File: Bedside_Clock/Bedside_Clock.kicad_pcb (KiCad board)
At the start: 4 copper layers, 177.8 x 68.6 mm, 213 parts, among them J1 USBC_USB2.0, SW1 COLOR, SW2 MODE, SW3 BOOT, SW4 RESET, U1 ESP32-C3-MINI-1, U2 USBLC6-2SC6, U3 VCNL4040M3OE, U4 SN74LVC2T45DCTR, U5 MCP1825S

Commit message: [Docs] Add Schematics and Renders Add Diodes, Switches, and Conns to BOM Need Resistors and Capacitors now
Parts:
- R5: value 1k3 -> 1k43
- moved R10 0.25 mm to (120.6, 71.4)
- moved R11 0.25 mm to (123.6, 71.4)
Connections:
- net Net-(J1-CC2) renamed /CC2
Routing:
- net +3V3: track 83.4 -> 84.2 mm
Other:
- board text added: "3V3"
- board text added: "5V"
- board text added: "GND"
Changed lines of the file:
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@@
 	(net 186 "Net-(D87-Pad2)")
 	(net 187 "/CC1")
-	(net 188 "Net-(J1-CC2)")
+	(net 188 "/CC2")
 	(net 189 "Net-(U1-GPIO8)")
 	(net 190 "/LED_BUILTIN")
@@
 			(size 0.3 1.1)
 			(layers "F.Cu" "F.Mask" "F.Paste")
-			(net 188 "Net-(J1-CC2)")
+			(net 188 "/CC2")
 			(pinfunction "CC2")
 			(pintype "bidirectional")
@@
 			(layers "F.Cu" "F.Mask" "F.Paste")
 			(roundrect_rratio 0.25)
-			(net 188 "Net-(J1-CC2)")
+			(net 188 "/CC2")
 			(pintype "passive")
 		)
@@
 			)
 		)
-		(property "Value" "1k3"
+		(property "Value" "1k43"
 			(at 0 -1.43 90)
 			(layer "B.Fab")
@@
 	(footprint "Resistor_SMD:R_0603_1608Metric"
 		(layer "B.Cu")
-		(at 120.587 71.628 180)
+		(at 120.587 71.374 180)
 		(descr "Resistor SMD 0603 (1608 Metric), square (rectangular) end terminal, IPC-7351 nominal, (Body size source: IPC-SM-782 page 72, https://www.pcb-3d.com/wordpress/wp-content/uploads/ipc-sm-782a_amendment_1_and_2.pdf), generated with kicad-footprint-generator")
 		(tags "resistor")
@@
 	(footprint "Resistor_SMD:R_0603_1608Metric"
 		(layer "B.Cu")
-		(at 123.634 71.628)
+		(at 123.634 71.374)
 		(descr "Resistor SMD 0603 (1608 Metric), square (rectangular) end terminal, IPC-7351 nominal, (Body size source: IPC-SM-782 page 72, https://www.pcb-3d.com/wordpress/wp-content/uploads/ipc-sm-782a_amendment_1_and_2.pdf), generated with kicad-footprint-generator")
 		(tags "resistor")
@@
 		(layer "User.2")
 	)
+	(gr_text "GND"
+		(at 116.0272 70.231 0)
+		(layer "B.SilkS")
+		(effects
+			(font
+				(size 1 1)
+				(thickness 0.15)
+			)
+			(justify right mirror)
+		)
+	)
+	(gr_text "3V3"
+		(at 116.0272 72.531 0)
+		(layer "B.SilkS")
+		(effects
+			(font
+				(size 1 1)
+				(thickness 0.15)
+			)
+			(justify right mirror)
+		)
+	)
+	(gr_text "5V"
+		(at 116.0272 67.931 0)
+		(layer "B.SilkS")
+		(effects
+			(font
+				(size 1 1)
+				(thickness 0.15)
+			)
+			(justify right mirror)
+		)
+	)
 	(segment
 		(start 133.78 50.66)
@@
 	)
 	(via
-		(at 125.349 71.628)
+		(at 125.222 71.374)
 		(size 0.6)
 		(drill 0.3)
@@
 	)
 	(via
-		(at 118.872 71.628)
+		(at 118.999 71.374)
 		(size 0.6)
 		(drill 0.3)
@@
 	)
 	(segment
-		(start 118.872 71.628)
-		(end 119.762 71.628)
+		(start 117.348 69.469)
+		(end 117.348 58.293)
+		(width 0.4)
+		(layer "B.Cu")
+		(net 181)
+	)
+	(segment
+		(start 124.459 71.374)
+		(end 125.222 71.374)
+		(width 0.4)
+		(layer "B.Cu")
+		(net 181)
+	)
+	(segment
+		(start 117.348 70.118)
+		(end 117.348 69.469)
+		(width 0.4)
+		(layer "B.Cu")
+		(net 181)
+	)
+	(segment
+		(start 114.935 72.531)
+		(end 117.842 72.531)
 		(width 0.4)
 		(layer "B.Cu")
@@
 	)
 	(segment
-		(start 119.448 54.356)
-		(end 117.869 54.356)
+		(start 117.348 69.977)
+		(end 117.348 69.723)
 		(width 0.4)
 		(layer "B.Cu")
@@
 	)
 	(segment
-		(start 117.969 72.531)
-		(end 114.935 72.531)
+		(start 117.348 69.723)
+		(end 117.348 69.469)
 		(width 0.4)
 		(layer "B.Cu")
@@
 	)
 	(segment
-		(start 87.995 85.699)
-		(end 87.995 84.104)
+		(start 119.448 54.356)
+		(end 117.869 54.356)
 		(width 0.4)
 		(layer "B.Cu")
@@
 	)
 	(segment
-		(start 118.3355 58.293)
-		(end 117.348 58.293)
+		(start 114.935 72.531)
+		(end 117.348 70.118)
 		(width 0.4)
 		(layer "B.Cu")
@@
 	)
 	(segment
-		(start 118.872 71.628)
-		(end 117.969 72.531)
+		(start 119.762 71.374)
+		(end 118.999 71.374)
 		(width 0.4)
 		(layer "B.Cu")
@@
 	)
 	(segment
-		(start 114.935 79.629)
-		(end 114.935 72.531)
-		(width 0.6)
+		(start 87.995 85.699)
+		(end 87.995 84.104)
+		(width 0.4)
 		(layer "B.Cu")
 		(net 181)
 	)
 	(segment
-		(start 117.348 70.104)
-		(end 117.348 58.293)
+		(start 117.842 72.531)
+		(end 118.999 71.374)
 		(width 0.4)
 		(layer "B.Cu")
@@
 	)
 	(segment
-		(start 114.935 72.531)
-		(end 114.935 72.517)
+		(start 118.3355 58.293)
+		(end 117.348 58.293)
 		(width 0.4)
 		(layer "B.Cu")
@@
 	)
 	(segment
-		(start 126.238 81.534)
-		(end 125.475 81.534)
+		(start 117.348 70.104)
+		(end 117.348 69.723)
 		(width 0.4)
 		(layer "B.Cu")
@@
 	)
 	(segment
-		(start 119.448 53.467)
-		(end 119.448 54.356)
+		(start 114.935 79.629)
+		(end 114.935 72.531)
+		(width 0.6)
+		(layer "B.Cu")
+		(net 181)
+	)
+	(segment
+		(start 114.935 72.531)
+		(end 114.935 72.517)
 		(width 0.4)
 		(layer "B.Cu")
@@
 	)
 	(segment
-		(start 125.349 71.628)
-		(end 124.459 71.628)
+		(start 126.238 81.534)
+		(end 125.475 81.534)
 		(width 0.4)
 		(layer "B.Cu")
@@
 	)
 	(segment
-		(start 118.872 71.628)
-		(end 117.348 70.104)
+		(start 119.448 53.467)
+		(end 119.448 54.356)
 		(width 0.4)
 		(layer "B.Cu")
@@
 	)
 	(segment
-		(start 114.935 72.517)
-		(end 117.348 70.104)
+		(start 117.348 54.877)
+		(end 117.869 54.356)
 		(width 0.4)
 		(layer "B.Cu")
@@
 	)
 	(segment
-		(start 117.348 54.877)
-		(end 117.869 54.356)
+		(start 118.999 71.374)
+		(end 117.348 69.723)
 		(width 0.4)
 		(layer "B.Cu")
@@
 	)
 	(segment
-		(start 125.349 71.628)
-		(end 118.872 71.628)
+		(start 125.222 71.374)
+		(end 118.999 71.374)
 		(width 0.4)
-		(layer "In2.Cu")
+		(layer "In1.Cu")
 		(net 181)
 	)

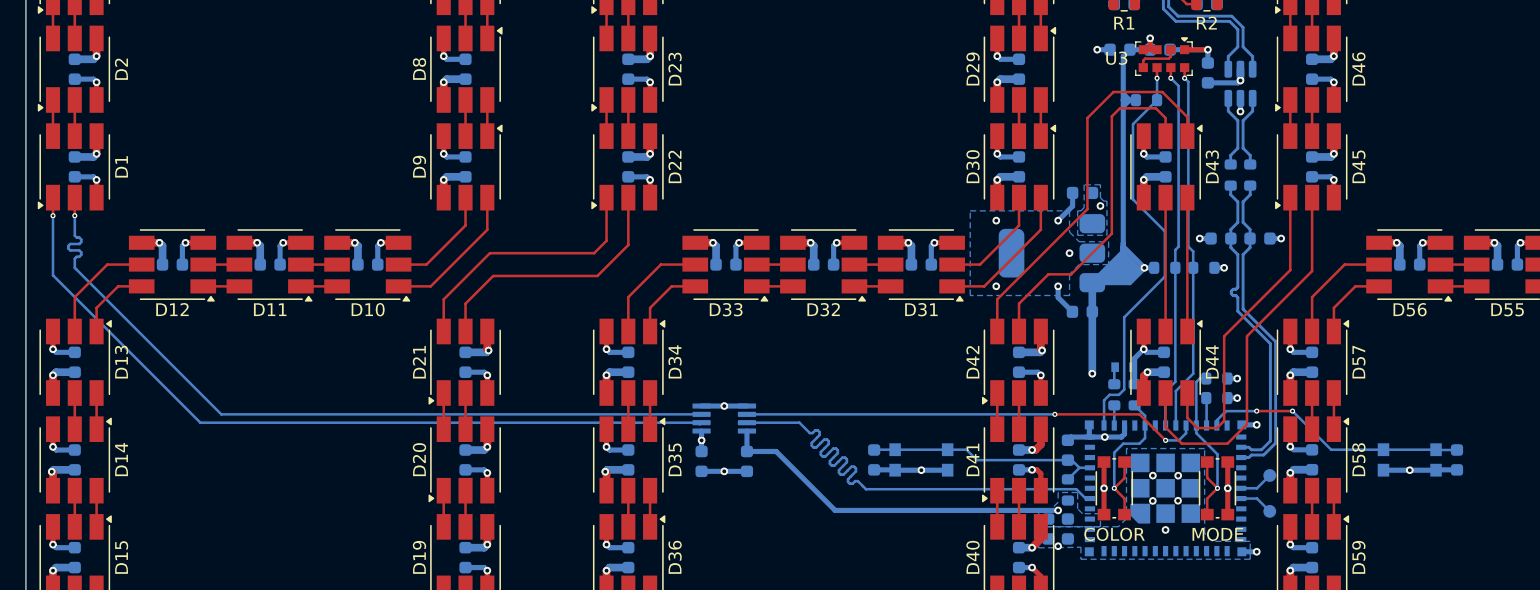
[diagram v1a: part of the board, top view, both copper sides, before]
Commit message: [HW] Add Series Resistors for SPI/LED Data (can be replaced with 0Ω if necessary) SPI Routing clean up to allow series resistors Also cleaned up some usage notes
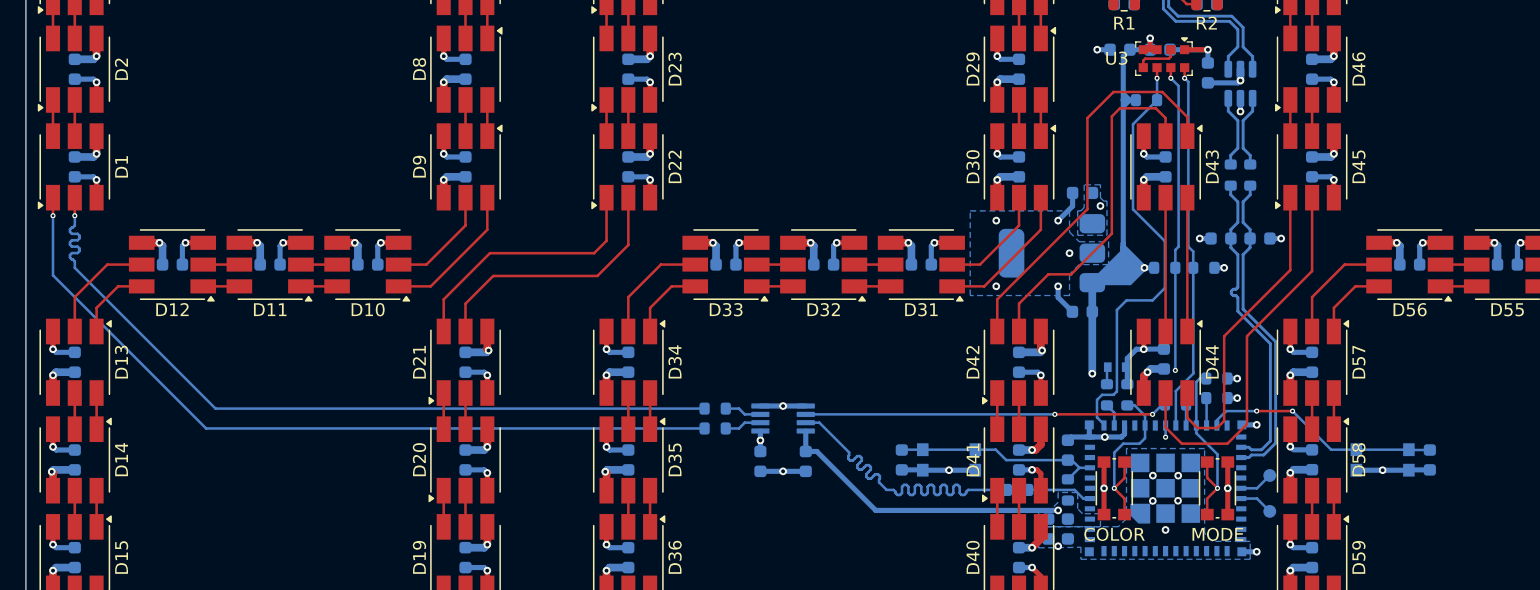
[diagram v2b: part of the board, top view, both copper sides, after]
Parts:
- added R13: 33, Resistor_SMD:R_0603_1608Metric, B.Cu at (109.1, 88.7)
- added R14: 33, Resistor_SMD:R_0603_1608Metric, B.Cu at (121.4, 82.0)
- added R15: 33, Resistor_SMD:R_0603_1608Metric, B.Cu at (85.5, 83.9)
- added R16: 33, Resistor_SMD:R_0603_1608Metric, B.Cu at (85.5, 82.4)
- C43: value 10uF -> 100nF
- R10, R11: value 2k2 -> 3k3
- moved C97 4.59 mm to (89.0, 86.5)
- moved U4 4.59 mm to (90.8, 83.1)
- moved C98 4.59 mm to (92.6, 86.5)
- moved SW4 2.16 mm to (103.8, 86.4)
- moved C96 2.16 mm to (100.1, 86.4)
- moved C95 2.12 mm to (141.3, 86.4)
- moved SW3 2.12 mm to (137.6, 86.4)
- moved D87 0.57 mm to (116.8, 79.1)
- moved R5 0.57 mm to (116.1, 81.3)
- moved R8 0.57 mm to (117.7, 81.3)
- moved C44 0.25 mm to (120.5, 78.5)
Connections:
- U1 pad 20: /CO -> /CO'
- U1 pad 5: /DO -> /DO'
- U4 pad 2: /Digit0/DI -> /DO''
- U4 pad 3: /Digit0/CI -> /CO''
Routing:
- net /DO: track 39.0 -> 27.9 mm
- net /CO: track 35.9 -> 28.3 mm
- net /DO': track 0.00 -> 5.10 mm
- net +3V3: track 84.2 -> 79.6 mm
- net /DO'': track 0.00 -> 2.89 mm
- net /CO'': track 0.00 -> 2.89 mm
- net /CHIP_EN: track 18.4 -> 16.2 mm
- net /BOOT: track 20.7 -> 18.6 mm
- net /SDA: track 28.6 -> 30.4 mm, vias 1 -> 3
- net /PROX_INT: track 32.1 -> 33.9 mm
- net /CO': track 0.00 -> 1.63 mm
- net /COLOR: track 13.3 -> 13.9 mm
